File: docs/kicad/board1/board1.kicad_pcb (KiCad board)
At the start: 2 copper layers, 95.2 x 61 mm, 45 parts, among them J1 12 IN, J2 SENSOR_ASSY, J3 5V Jump, J4 5V Test, J5 TEST_A, J6 TEST_B, J7 WS2812_B, J8 PUMP, M1 BUCK01, Q1 IRF520N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

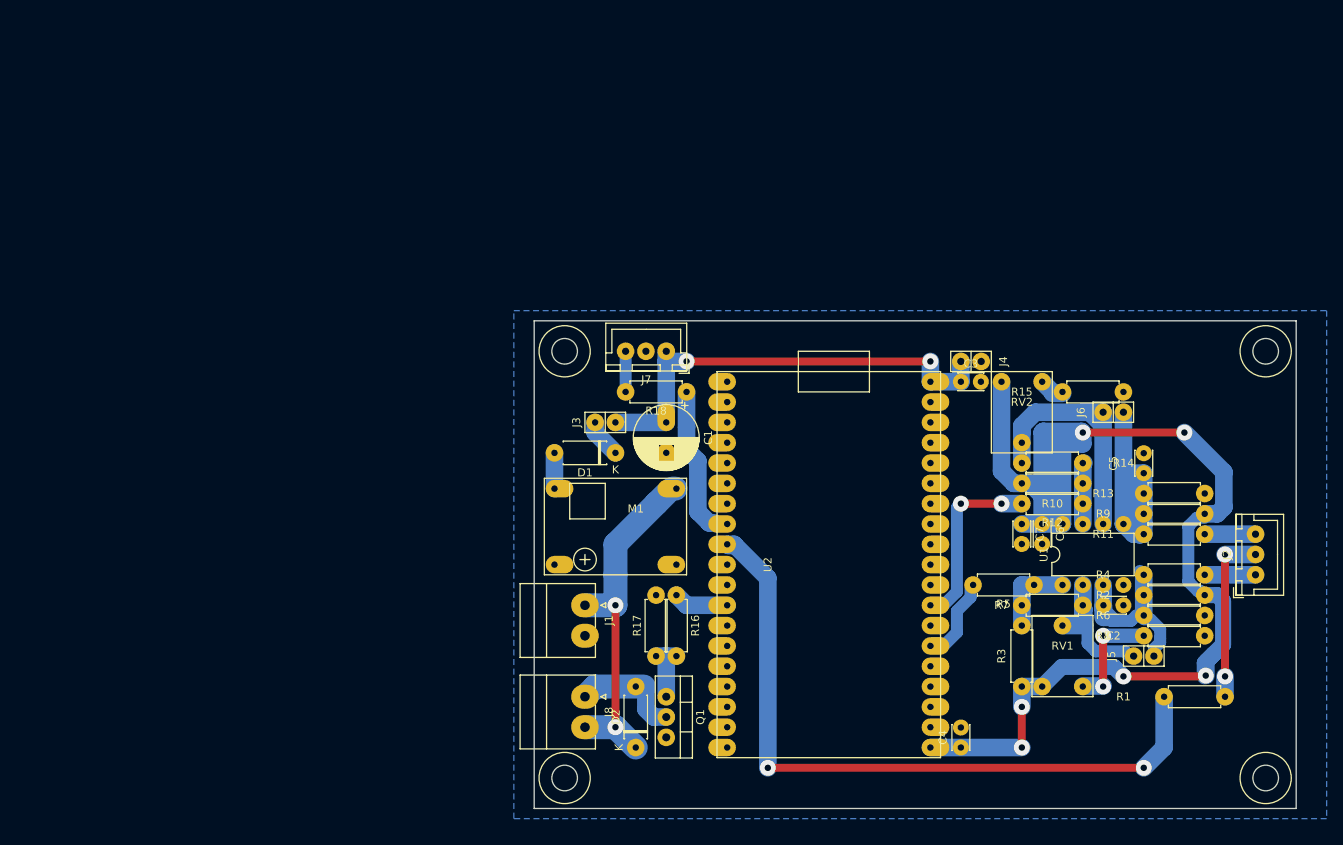
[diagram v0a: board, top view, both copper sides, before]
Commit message: finish drainPump PCB and myIOT implementation
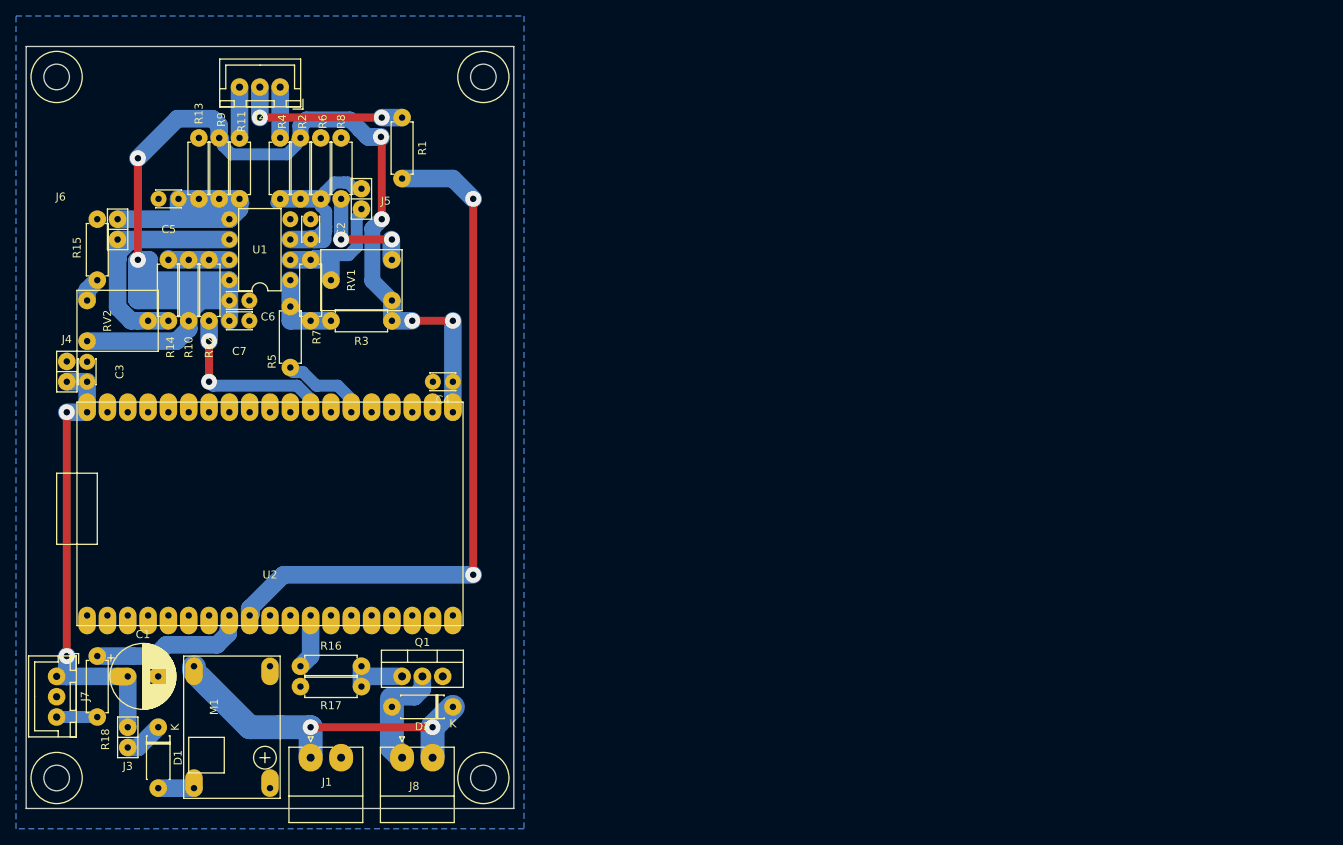
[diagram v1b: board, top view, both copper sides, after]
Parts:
- removed the REF** at (181.6, 113.0)
- removed the REF** at (94.0, 113.0)
- removed the REF** at (94.0, 59.7)
- added REF**: myMountingHole_3.2mm_M3, 0_my_footprints:myMountingHole_3.2mm_M3, F.Cu at (83.8, 25.4)
- added REF**: myMountingHole_3.2mm_M3, 0_my_footprints:myMountingHole_3.2mm_M3, F.Cu at (83.8, 113.0)
- added REF**: myMountingHole_3.2mm_M3, 0_my_footprints:myMountingHole_3.2mm_M3, F.Cu at (30.5, 113.0)
- C2, C5: value 33nf -> 1uf
- J5: value TEST_A -> TEST_LOW
- J6: value TEST_B -> TEST_HIGH
- R10, R15, R3, R8: value 10k -> 4.7K
- R13, R6: value 100K -> 47K
- R14, R7: value 220K -> 100K
- RV1, RV2: value 200K -> 100K
- moved REF** 155.0 mm to (30.5, 25.4), turned to 90 degrees
- moved J2 136.3 mm to (58.4, 26.7), turned to 180 degrees
- moved R9 131.8 mm to (50.8, 33.0), turned to 270 degrees
- moved R11 130.4 mm to (53.3, 33.0), turned to 270 degrees
- moved R4 127.8 mm to (58.4, 33.0), turned to 270 degrees
- moved R2 126.7 mm to (61.0, 33.0), turned to 270 degrees
- moved R1 125.8 mm to (73.7, 30.5), turned to 270 degrees
- moved C5 125.4 mm to (45.7, 40.6), turned to 180 degrees
- moved J6 125.1 mm to (38.1, 45.7), turned to 180 degrees
- moved R13 123.7 mm to (48.3, 40.6), turned to 90 degrees
- moved R15 121.5 mm to (35.6, 50.8), turned to 90 degrees
- moved RV2 117.1 mm to (34.3, 55.9), turned to 270 degrees
- moved R6 115.3 mm to (63.5, 40.6), turned to 90 degrees
- moved J4 114.3 mm to (31.8, 61.0), turned to 0 degrees
- moved R8 114.2 mm to (66.0, 40.6), turned to 90 degrees
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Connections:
- net INPUT_A renamed INPUT_LOW
- net INPUT_B renamed INPUT_HIGH
- net ROD_A renamed ROD_LOW
- net ROD_B renamed ROD_HIGH
- net SENSOR_A renamed SENSOR_LOW
- net SENSOR_B renamed SENSOR_HIGH
- net THRESH_A renamed THRESH_LOW
- net THRESH_B renamed THRESH_HIGH
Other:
- board size 95.2 x 61 mm -> 61 x 95.2 mm
